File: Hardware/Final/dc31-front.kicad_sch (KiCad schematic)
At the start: 10 parts

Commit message: Almost final, still need some artwork
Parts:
- added J7: FRONT, Connector_PinSocket_2.54mm:PinSocket_1x04_P2.54mm_Vertical_SMD_Pin1Left, symbol Connector_Generic:Conn_01x04
- added R101: 10R, Resistor_SMD:R_0603_1608Metric, symbol Device:R
- D101: renamed from D1; footprint LED_SMD:LED_WS2812B_PLCC4_5.0x5.0mm_P3.2mm -> lib_fp:LED_SK6812_4020_; symbol LED:WS2812B -> SK6812-SIDE:SK6812-SIDE
- D102: renamed from D2; footprint LED_SMD:LED_WS2812B_PLCC4_5.0x5.0mm_P3.2mm -> lib_fp:LED_SK6812_4020_; symbol LED:WS2812B -> SK6812-SIDE:SK6812-SIDE
- D103: renamed from D3; footprint LED_SMD:LED_WS2812B_PLCC4_5.0x5.0mm_P3.2mm -> lib_fp:LED_SK6812_4020_; symbol LED:WS2812B -> SK6812-SIDE:SK6812-SIDE
- D104: renamed from D4; footprint LED_SMD:LED_WS2812B_PLCC4_5.0x5.0mm_P3.2mm -> lib_fp:LED_SK6812_4020_; symbol LED:WS2812B -> SK6812-SIDE:SK6812-SIDE
- D105: renamed from D5; footprint LED_SMD:LED_WS2812B_PLCC4_5.0x5.0mm_P3.2mm -> lib_fp:LED_SK6812_4020_; symbol LED:WS2812B -> SK6812-SIDE:SK6812-SIDE
- D106: renamed from D6; footprint LED_SMD:LED_WS2812B_PLCC4_5.0x5.0mm_P3.2mm -> lib_fp:LED_SK6812_4020_; symbol LED:WS2812B -> SK6812-SIDE:SK6812-SIDE
- D107: renamed from D7; footprint LED_SMD:LED_WS2812B_PLCC4_5.0x5.0mm_P3.2mm -> lib_fp:LED_SK6812_4020_; symbol LED:WS2812B -> SK6812-SIDE:SK6812-SIDE
- D108: renamed from D8; footprint LED_SMD:LED_WS2812B_PLCC4_5.0x5.0mm_P3.2mm -> lib_fp:LED_SK6812_4020_; symbol LED:WS2812B -> SK6812-SIDE:SK6812-SIDE
- D109: renamed from D9; footprint LED_SMD:LED_WS2812B_PLCC4_5.0x5.0mm_P3.2mm -> lib_fp:LED_SK6812_4020_; symbol LED:WS2812B -> SK6812-SIDE:SK6812-SIDE
- D110: renamed from D10; footprint LED_SMD:LED_WS2812B_PLCC4_5.0x5.0mm_P3.2mm -> lib_fp:LED_SK6812_4020_; symbol LED:WS2812B -> SK6812-SIDE:SK6812-SIDE
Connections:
- net RGB_IN is gone; now on net GND: D101.4 (VSS)
- net GND: now also D102.4 (VSS), D103.4 (VSS), D104.4 (VSS), D105.4 (VSS), D106.4 (VSS), D107.4 (VSS), D108.4 (VSS), D109.4 (VSS), D110.4 (VSS), J7.1 (Pin_1); no longer D101.3 (VSS), D102.3 (VSS), D103.3 (VSS), D104.3 (VSS), D105.3 (VSS), D106.3 (VSS), D107.3 (VSS), D108.3 (VSS), D109.3 (VSS), D110.3 (VSS)
- net +3V3: now reaches D101.2 (VDD)
- net +3V3: now also D102.2 (VDD), D103.2 (VDD), D104.2 (VDD), D105.2 (VDD), D106.2 (VDD), D107.2 (VDD), D108.2 (VDD), D109.2 (VDD), D110.2 (VDD), J7.2 (Pin_2); no longer D102.4 (DIN)
- removed net VBUS: D101.1 (VDD), D102.1 (VDD), D103.1 (VDD), D104.1 (VDD), D105.1 (VDD), D106.1 (VDD), D107.1 (VDD), D108.1 (VDD), D109.1 (VDD), D110.1 (VDD)
- new net: D101.1 (DIN), R101.1
- new net: D101.3 (DOUT), D102.1 (DIN)
- new net: J7.4 (Pin_4), R101.2
- new net: D102.3 (DOUT), D103.1 (DIN)
- new net: D106.3 (DOUT), D107.1 (DIN)
- new net: D107.3 (DOUT), D108.1 (DIN)
- new net: D103.3 (DOUT), D104.1 (DIN)
- new net: D104.3 (DOUT), D105.1 (DIN)
- new net: D108.3 (DOUT), D109.1 (DIN)
- new net: D109.3 (DOUT), D110.1 (DIN)
- new net: D105.3 (DOUT), D106.1 (DIN)
- no-connect marks 0 -> 1
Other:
- company: (none) -> DCZia
- title: (none) -> DCZia Electric Sampler
- moved on the sheet: D101, D102, D103, D104, D105, D106, D107, D108, D109, D110

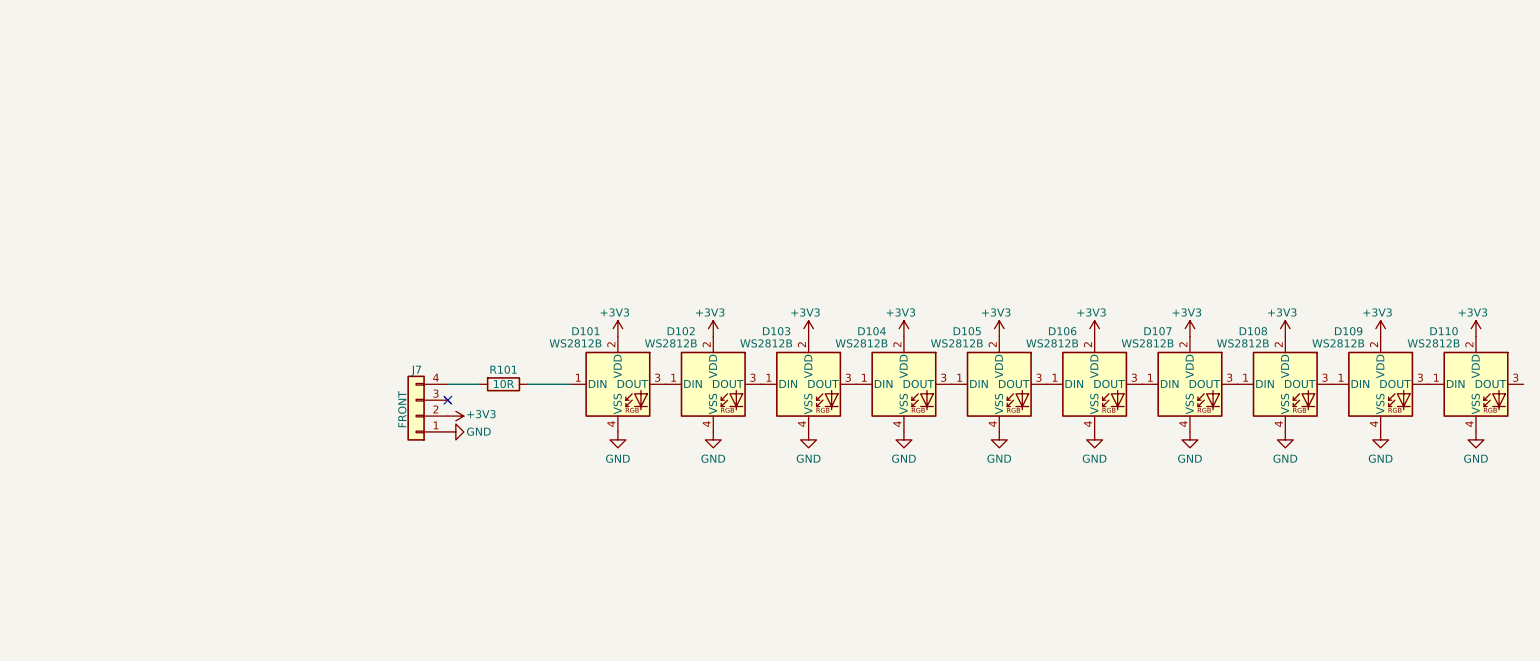
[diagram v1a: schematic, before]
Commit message: Adding SAO port to front panel Adding hamster art to boards A few more small tweaks before final export
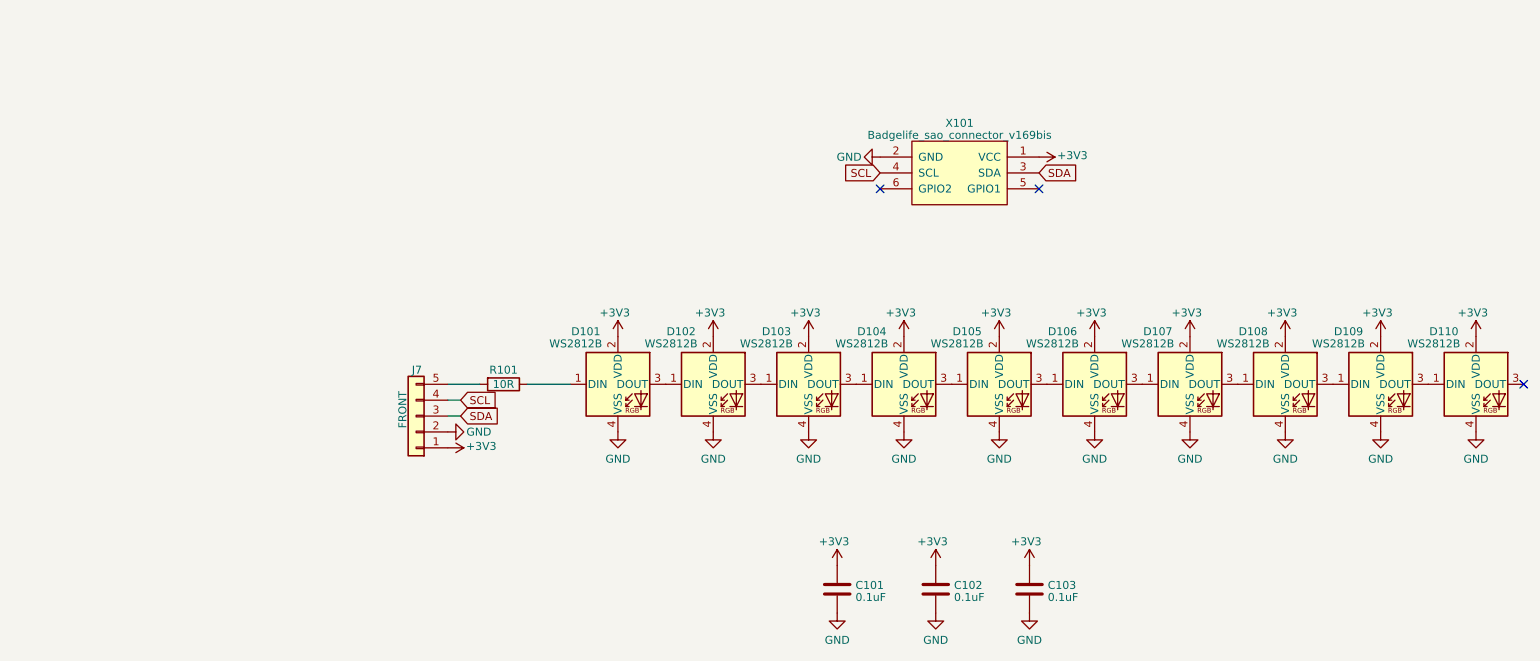
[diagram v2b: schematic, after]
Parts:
- removed J7: FRONT, Connector_PinSocket_2.54mm:PinSocket_1x04_P2.54mm_Vertical_SMD_Pin1Left, symbol Connector_Generic:Conn_01x04
- added C101, C102, C103: 0.1uF, Capacitor_SMD:C_0603_1608Metric, symbol Device:C
- added J7: FRONT, Connector_PinSocket_2.54mm:PinSocket_1x05_P2.54mm_Vertical_SMD_Pin1Left, symbol Connector_Generic:Conn_01x05
- added X101: Badgelife_sao_connector_v169bis, lib_fp:Badgelife-Shitty-v1.69bis, symbol badgelife_shitty_addon_v169bis:Badgelife_sao_connector_v169bis
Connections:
- net +3V3: now also C101.1, C102.1, C103.1, J7.1 (Pin_1), X101.1 (VCC)
- net GND: now also C101.2, C102.2, C103.2, J7.2 (Pin_2), X101.2 (GND)
- net at R101.2: now also J7.5 (Pin_5)
- new net SCL: J7.4 (Pin_4), X101.4 (SCL)
- new net SDA: J7.3 (Pin_3), X101.3 (SDA)
- no-connect marks 1 -> 3
